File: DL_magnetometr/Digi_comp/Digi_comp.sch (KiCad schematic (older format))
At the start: 49 parts, among them J1 USB_B_Micro, U1 AP7331-WG-7, U2 74AHCT1G125, U3 JST-PHR-2, U4 AZ4558CM, U5 AZ4558CM, U6 AP7331-WG-7, Y1 32.768k, Y2 16M/32M

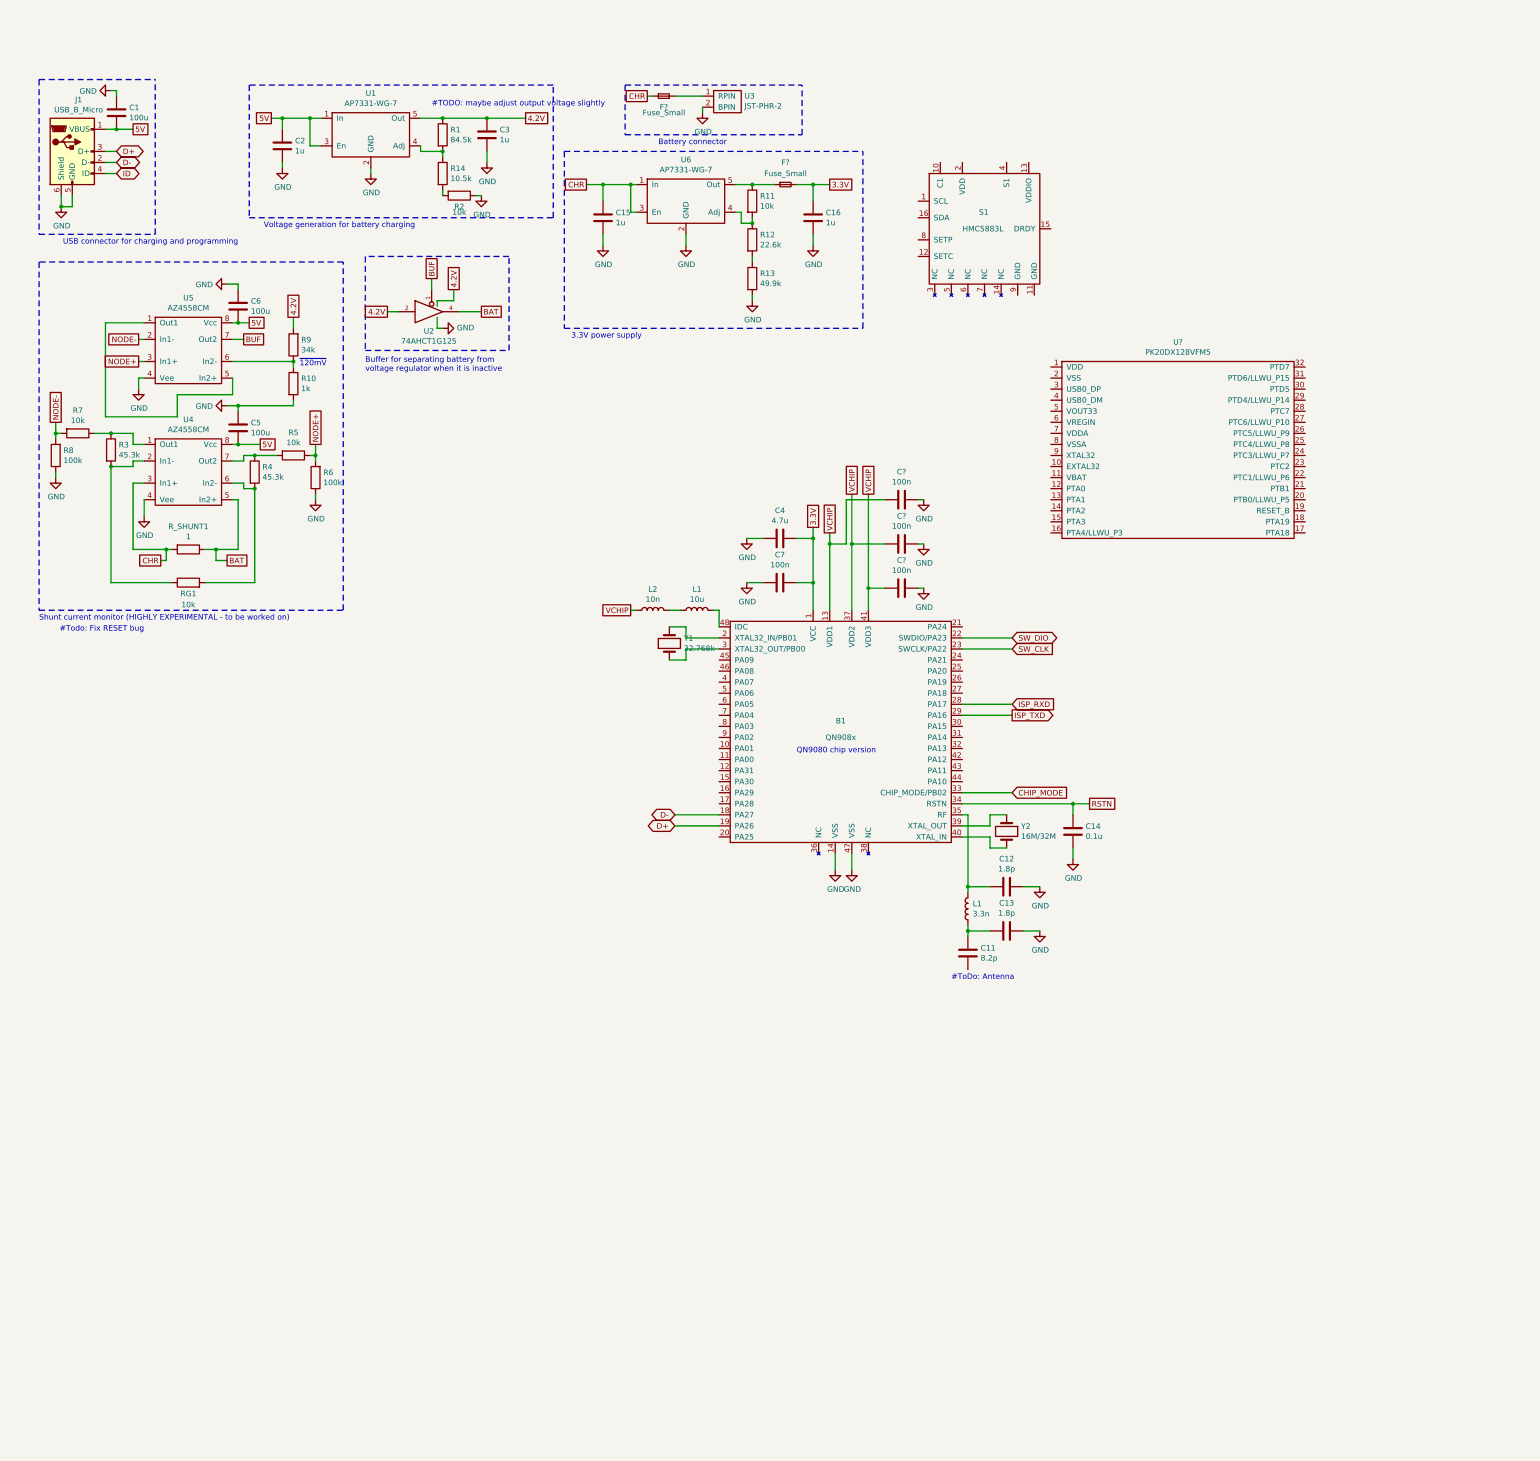
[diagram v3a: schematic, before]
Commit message: Added ESD protection circuitry
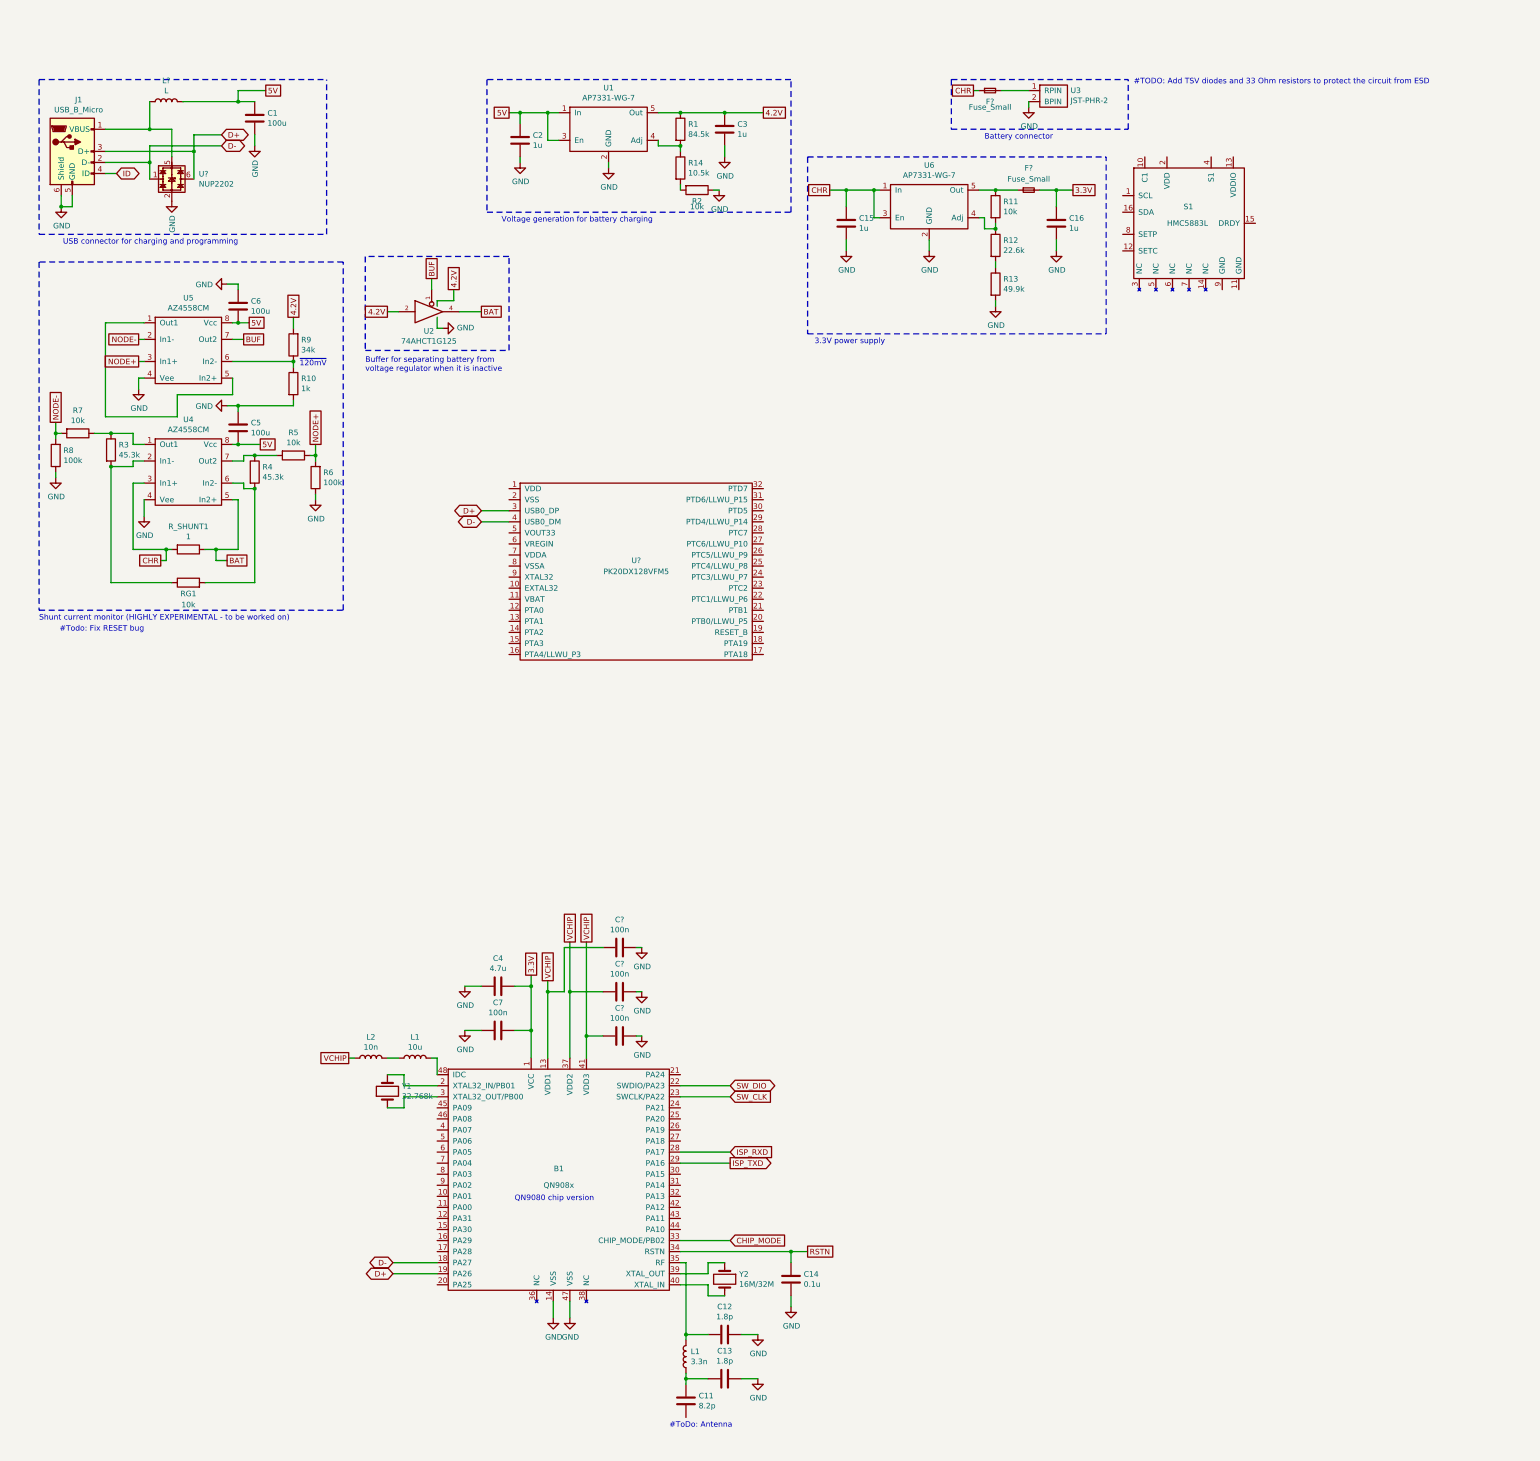
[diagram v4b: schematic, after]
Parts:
- added L?: L, symbol Device:L
- added U?: NUP2202, Package_TO_SOT_SMD:SOT-363_SC-70-6, symbol Power_Protection:NUP2202
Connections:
- net 5V: now also C1.1, L?.2; no longer C1.2, J1.1 (VBUS)
- net D+: now also U?.3 (USB0_DP), U?.6
- net D-: now also U?.4 (USB0_DM), U?.1
- net GND: now also C1.2, U?.2; no longer C1.1
- new net: J1.1 (VBUS), L?.1, U?.5
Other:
- note added: "#TODO: Add TSV diodes and 33 Ohm resistors to protect the circuit from ESD"
- note removed: "#TODO: maybe adjust output voltage slightly"
- moved on the sheet: B1, C1, C11, C12, C13, C14, C15, C16, C2, C3, C4, C7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

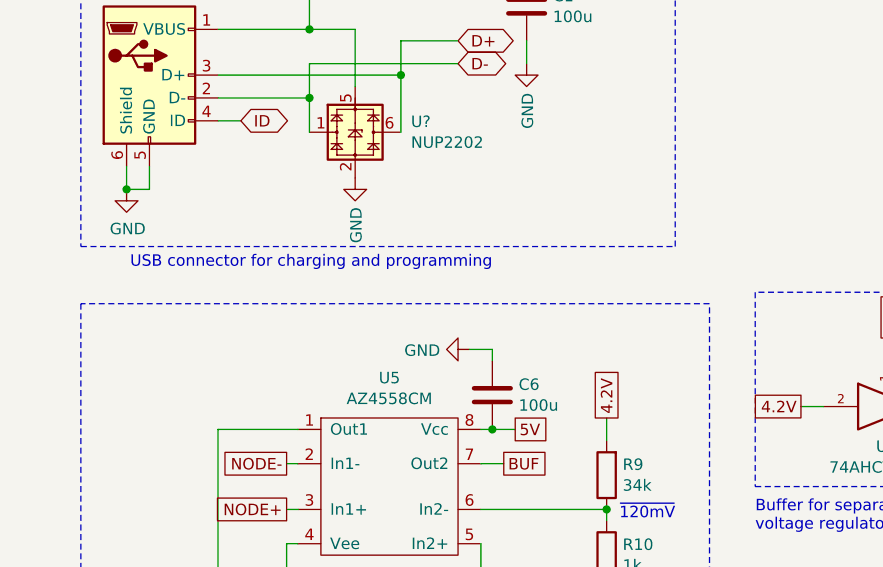
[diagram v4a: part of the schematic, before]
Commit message: Added #TODO comments
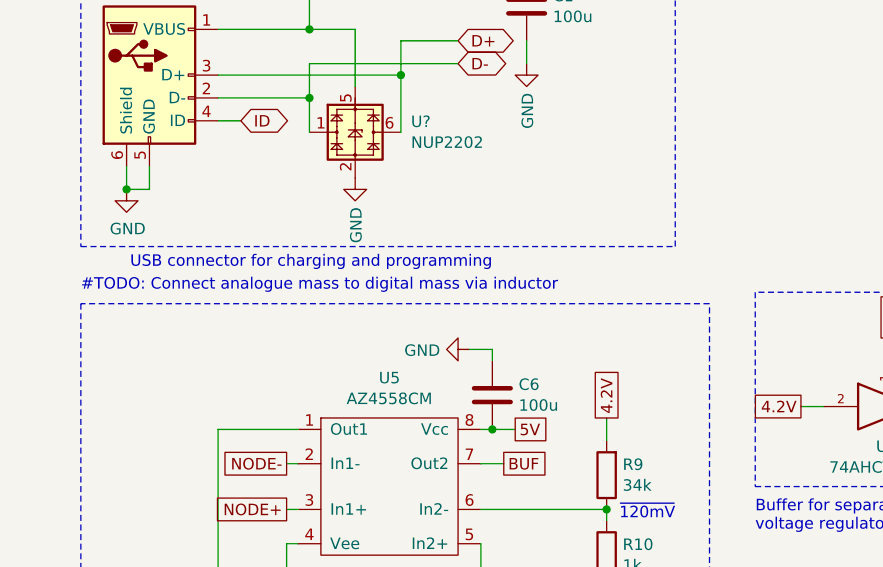
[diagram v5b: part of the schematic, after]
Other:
- note added: "#TODO: Connect analogue mass to digital mass via inductor"
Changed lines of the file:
@@
 Wire Notes Line
 	500  550  3100 550
+Text Notes 500  2150 0    50   ~ 0
+#TODO: Connect analogue mass to digital mass via inductor
 $EndSCHEMATC

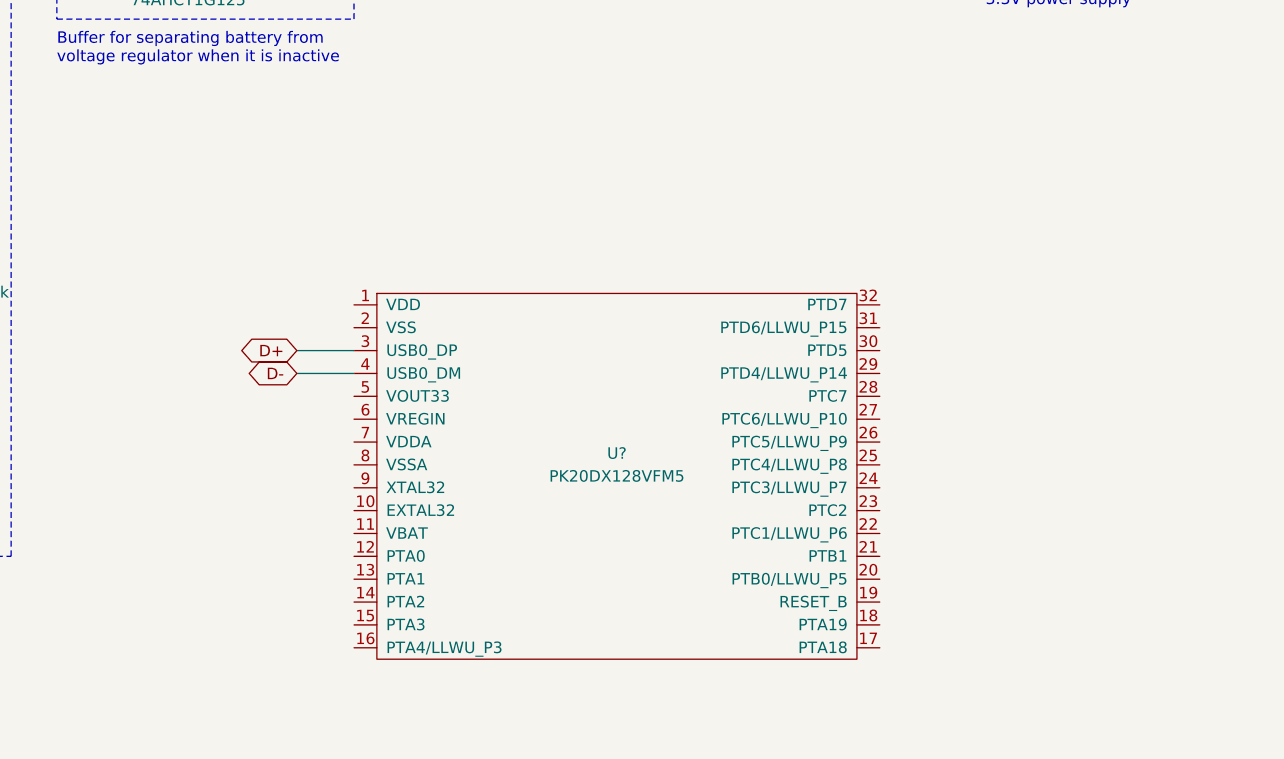
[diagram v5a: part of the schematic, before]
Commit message: Prototype of programming unit added
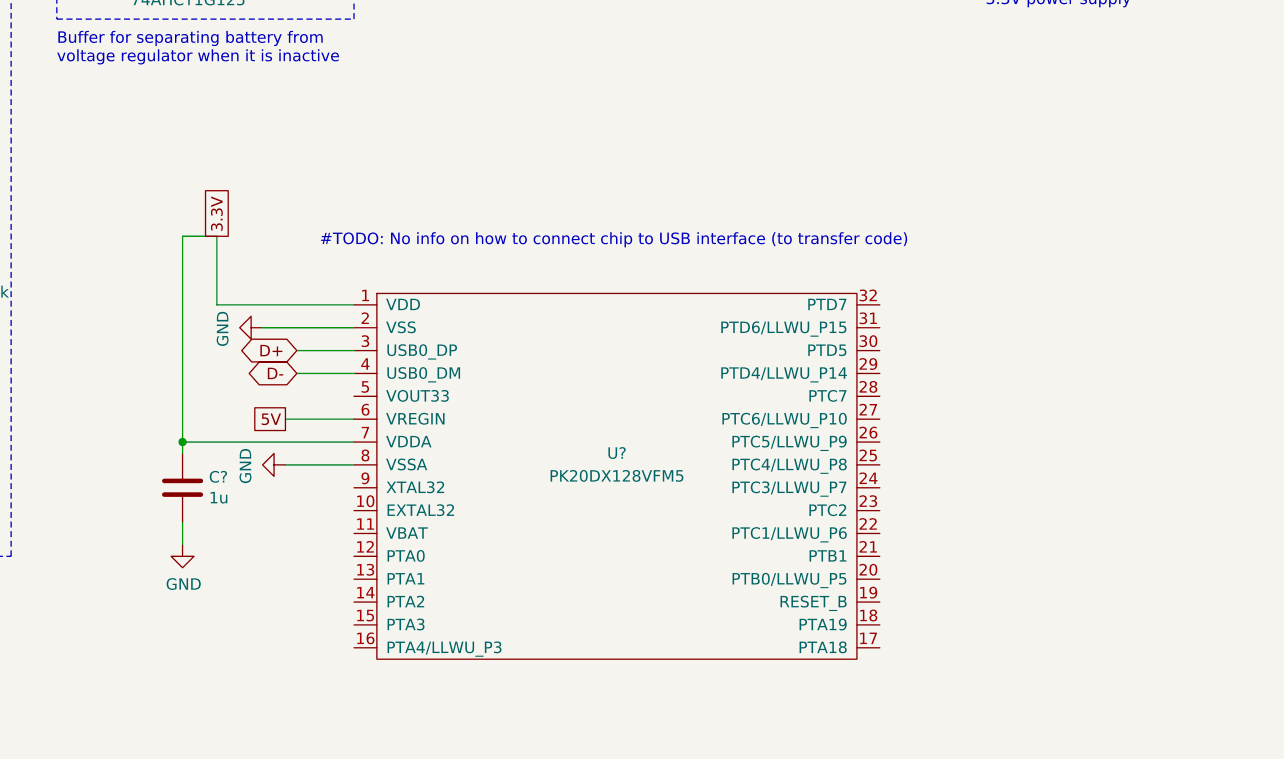
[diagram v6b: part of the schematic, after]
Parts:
- added C?: 1u, symbol Device:C
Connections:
- net 3.3V: now also U?.1 (VDD), U?.7 (VDDA), C?.1
- net 5V: now also U?.6 (VREGIN)
- net GND: now also U?.2 (VSS), U?.8 (VSSA), C?.2
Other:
- note added: "#TODO: No info on how to connect chip to USB interface (to transfer code)"
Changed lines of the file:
@@
 Text Notes 500  2150 0    50   ~ 0
 #TODO: Connect analogue mass to digital mass via inductor
+Text GLabel 4450 4750 0    50   UnSpc ~ 0
+5V
+Wire Wire Line
+	4450 4750 4750 4750
+$Comp
+L power:GND #PWR?
+U 1 1 5FEC0074
+P 4350 4350
+F 0 "#PWR?" H 4350 4100 50  0001 C CNN
+F 1 "GND" H 4355 4177 50  0000 C CNN
+F 2 "" H 4350 4350 50  0001 C CNN
+F 3 "" H 4350 4350 50  0001 C CNN
+	1    4350 4350
+	0    1    1    0
+$EndComp
+Wire Wire Line
+	4350 4350 4750 4350
+Text GLabel 4150 3950 1    50   UnSpc ~ 0
+3.3V
+$Comp
+L Device:C C?
+U 1 1 5FECB487
+P 4000 5050
+F 0 "C?" H 4115 5096 50  0000 L CNN
+F 1 "1u" H 4115 5005 50  0000 L CNN
+F 2 "" H 4038 4900 50  0001 C CNN
+F 3 "~" H 4000 5050 50  0001 C CNN
+	1    4000 5050
+	1    0    0    -1
+$EndComp
+Wire Wire Line
+	4750 4850 4000 4850
+Wire Wire Line
+	4000 4850 4000 4900
+Wire Wire Line
+	4150 3950 4000 3950
+Wire Wire Line
+	4000 3950 4000 4850
+Connection ~ 4000 4850
+Wire Wire Line
+	4150 3950 4150 4250
+Wire Wire Line
+	4150 4250 4750 4250
+$Comp
+L power:GND #PWR?
+U 1 1 5FEED2D3
+P 4000 5300
+F 0 "#PWR?" H 4000 5050 50  0001 C CNN
+F 1 "GND" H 4005 5127 50  0000 C CNN
+F 2 "" H 4000 5300 50  0001 C CNN
+F 3 "" H 4000 5300 50  0001 C CNN
+	1    4000 5300
+	1    0    0    -1
+$EndComp
+Wire Wire Line
+	4000 5300 4000 5200
+$Comp
+L power:GND #PWR?
+U 1 1 5FEF8CB1
+P 4450 4950
+F 0 "#PWR?" H 4450 4700 50  0001 C CNN
+F 1 "GND" H 4455 4777 50  0000 C CNN
+F 2 "" H 4450 4950 50  0001 C CNN
+F 3 "" H 4450 4950 50  0001 C CNN
+	1    4450 4950
+	0    1    1    0
+$EndComp
+Wire Wire Line
+	4450 4950 4750 4950
+Text Notes 4600 4000 0    50   ~ 0
+#TODO: No info on how to connect chip to USB interface (to transfer code)
 $EndSCHEMATC

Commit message: Estetic changes
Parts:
- U8: renamed from U?; symbol CPU:PK20DX128VFM5 -> Digi_comp-rescue:PK20DX128VFM5-CPU
- gave numbers to parts that had none: 8
- renumbered L1 to L3
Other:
- note added: "Bluetooth communication module"
